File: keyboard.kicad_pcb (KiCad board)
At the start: 2 copper layers, 86 x 125 mm, 40 parts, among them M2_1 MountingHole_2.2mm_M2_ISO7380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, M2_2 MountingHole_2.2mm_M2_ISO7380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, M2_3 MountingHole_2.2mm_M2_ISO7380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, M2_4 MountingHole_2.2mm_M2_ISO7380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, M2_5 MountingHole_2.2mm_M2_ISO7380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, U1 nice_nano

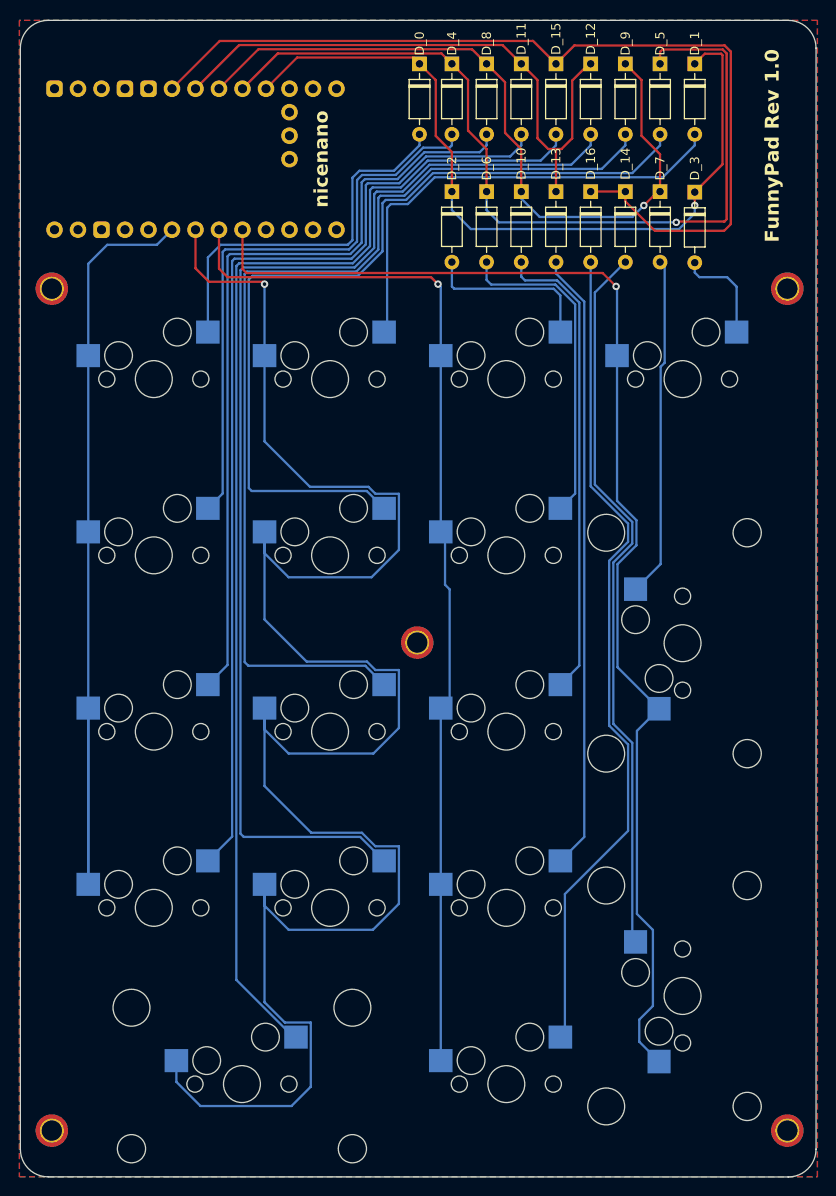
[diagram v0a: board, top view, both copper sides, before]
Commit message: Adjusted M2 screw position and board size to 86*125mm
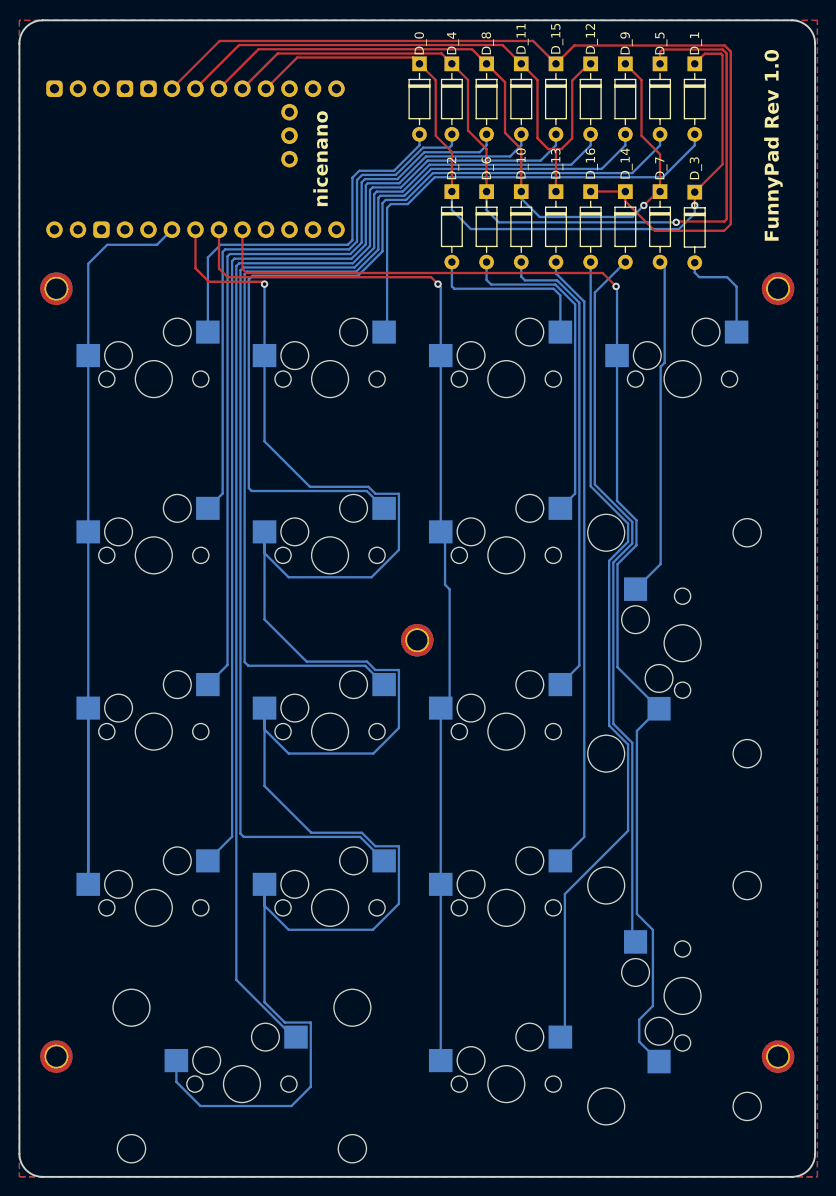
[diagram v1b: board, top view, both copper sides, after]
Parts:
- moved M2_5 8.06 mm to (327.5, 237.0)
- moved M2_4 8.02 mm to (249.5, 237.0)
- moved M2_2 1.00 mm to (327.5, 154.0)
- moved M2_1 0.50 mm to (249.5, 154.0)
- moved M2_3 0.25 mm to (288.5, 192.0)
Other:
- outline, holes or cut-outs redrawn
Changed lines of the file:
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@@
 			(psa4output no)
 			(plotreference yes)
-			(plotvalue yes)
+			(plotvalue no)
 			(plotfptext yes)
 			(plotinvisibletext no)
@@
 	(footprint "MountingHole:MountingHole_2.2mm_M2_ISO7380_Pad_TopBottom"
 		(layer "F.Cu")
-		(at 249 245)
+		(at 249.5 237)
 		(descr "Mounting Hole 2.2mm, M2, ISO7380")
 		(tags "mounting hole 2.2mm m2 iso7380")
@@
 	(footprint "MountingHole:MountingHole_2.2mm_M2_ISO7380_Pad_TopBottom"
 		(layer "F.Cu")
-		(at 328.5 154)
+		(at 327.5 154)
 		(descr "Mounting Hole 2.2mm, M2, ISO7380")
 		(tags "mounting hole 2.2mm m2 iso7380")
@@
 	(footprint "MountingHole:MountingHole_2.2mm_M2_ISO7380_Pad_TopBottom"
 		(layer "F.Cu")
-		(at 249 154)
+		(at 249.5 154)
 		(descr "Mounting Hole 2.2mm, M2, ISO7380")
 		(tags "mounting hole 2.2mm m2 iso7380")
@@
 	(footprint "MountingHole:MountingHole_2.2mm_M2_ISO7380_Pad_TopBottom"
 		(layer "F.Cu")
-		(at 328.5 245)
+		(at 327.5 237)
 		(descr "Mounting Hole 2.2mm, M2, ISO7380")
 		(tags "mounting hole 2.2mm m2 iso7380")
@@
 	(footprint "MountingHole:MountingHole_2.2mm_M2_ISO7380_Pad_TopBottom"
 		(layer "F.Cu")
-		(at 288.5 192.25)
+		(at 288.5 192)
 		(descr "Mounting Hole 2.2mm, M2, ISO7380")
 		(tags "mounting hole 2.2mm m2 iso7380")
@@
 		)
 	)
-	(gr_arc
-		(start 331.6 247.01066)
-		(mid 330.72132 249.13198)
-		(end 328.6 250.01066)
+	(gr_line
+		(start 329 250)
+		(end 248 250)
 		(stroke
-			(width 0.1)
+			(width 0.2)
 			(type default)
 		)
 		(layer "Edge.Cuts")
 	)
-	(gr_line
-		(start 248.599999 250.000001)
-		(end 328.6 250.01066)
+	(gr_arc
+		(start 248 250)
+		(mid 246.232233 249.267767)
+		(end 245.5 247.5)
 		(stroke
-			(width 0.1)
+			(width 0.2)
 			(type default)
 		)
 		(layer "Edge.Cuts")
 	)
-	(gr_arc
-		(start 248.599999 250.000001)
-		(mid 246.478679 249.121321)
-		(end 245.599999 247.000001)
+	(gr_line
+		(start 331.5 127.5)
+		(end 331.5 247.5)
 		(stroke
-			(width 0.1)
+			(width 0.2)
 			(type default)
 		)
@@
 	)
 	(gr_arc
-		(start 245.6 128)
-		(mid 246.47868 125.87868)
-		(end 248.6 125)
+		(start 245.5 127.5)
+		(mid 246.232233 125.732233)
+		(end 248 125)
 		(stroke
-			(width 0.1)
+			(width 0.2)
 			(type default)
 		)
@@
 	)
 	(gr_arc
-		(start 328.6 125)
-		(mid 330.72132 125.87868)
-		(end 331.6 128)
+		(start 329 125)
+		(mid 330.767767 125.732233)
+		(end 331.5 127.5)
 		(stroke
-			(width 0.1)
+			(width 0.2)
 			(type default)
 		)
@@
 	)
 	(gr_line
-		(start 331.6 128)
-		(end 331.6 247.01066)
+		(start 245.5 247.5)
+		(end 245.5 127.5)
 		(stroke
-			(width 0.1)
+			(width 0.2)
 			(type default)
 		)
 		(layer "Edge.Cuts")
 	)
-	(gr_line
-		(start 248.6 125)
-		(end 328.6 125)
+	(gr_arc
+		(start 331.5 247.5)
+		(mid 330.767767 249.267767)
+		(end 329 250)
 		(stroke
-			(width 0.1)
+			(width 0.2)
 			(type default)
 		)
@@
 	)
 	(gr_line
-		(start 245.6 128)
-		(end 245.599999 247.000001)
+		(start 248 125)
+		(end 329 125)
 		(stroke
-			(width 0.1)
+			(width 0.2)
 			(type default)
 		)
